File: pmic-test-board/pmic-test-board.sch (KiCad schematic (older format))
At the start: 53 parts

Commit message: more schematic capture
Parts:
- added C106: DNP, Capacitor_SMD:C_0603_1608Metric, symbol Device:C
- added C? (x2): 4.7u, Capacitor_SMD:C_0603_1608Metric, symbol Device:C
- added J?: Conn_02x09_Odd_Even, symbol Connector_Generic:Conn_02x09_Odd_Even
- added J?: Conn_Coaxial, symbol Connector:Conn_Coaxial
- added R?: 1k, Resistor_SMD:R_0603_1608Metric, symbol Device:R
- added R? (x6): 4.7k, symbol Device:R
- added R? (x4): 100, symbol Device:R
- C101: renamed from C?; footprint (none) -> Capacitor_SMD:C_0603_1608Metric
- C102: renamed from C?; footprint (none) -> Capacitor_Tantalum_SMD:CP_EIA-3528-12_Kemet-T; MPN (none) -> T520B476M008ATE035
- C104: renamed from C?; value C -> 5.1n; footprint (none) -> Capacitor_SMD:C_0603_1608Metric
- C105: renamed from C?; value C -> 220p; footprint (none) -> Capacitor_SMD:C_0603_1608Metric
- D101, D102, D103, D104, D105, D106: renamed from D?; footprint (none) -> LED_SMD:LED_0603_1608Metric_Castellated
- D107, D108: renamed from D?; value D_Schottky -> B0520WS-7-F; footprint (none) -> Diode_SMD:D_SOD-323; MPN (none) -> B0520WS-7-F
- L101: renamed from L?; value L -> 22u; MPN (none) -> LPS6235-223MRC
- Q101, Q102, Q103, Q104: renamed from Q?; footprint (none) -> Package_TO_SOT_SMD:SOT-23
- R101, R102, R103, R104, R105, R106, R107, R108, R109, R110, R111, R112, R113, R114, R115, R116, R117, R118, R119: renamed from R?; footprint (none) -> Resistor_SMD:R_0603_1608Metric
- R120: renamed from R?; value R -> 17.6k; footprint (none) -> Resistor_SMD:R_0603_1608Metric
- R121: renamed from R?; value R -> 40k; footprint (none) -> Resistor_SMD:R_0603_1608Metric
- R122: renamed from R?; value R -> 7.8k; footprint (none) -> Resistor_SMD:R_0603_1608Metric
- U101, U102: renamed from U?; footprint (none) -> Package_TO_SOT_SMD:SOT-363_SC-70-6
- U103: renamed from U?; MPN (none) -> W25Q32JVSSIQ
- gave numbers to parts that had none: 11
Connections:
- net +3V3: now also U103.8 (VCC), C?.1, C?.1
- net GND: now also U103.4 (GND), C106.2, C?.2, C?.2, J?.1 (In), R?.1, R?.1, R?.1, R?.1, R?.1, R?.1
- net vsw: now also D107.2 (A), D108.1 (K), L101.1, R119.1, J?.2 (Ext)
- net at U103.1 (~CS): now also R?.1, R?.2
- net at U103.2 (DO(IO1)): now also R?.2, R?.2
- net at U103.3 (IO2): now also R?.2
- net at U103.5 (DI(IO0)): now also R?.2, R?.2
- net at U103.6 (CLK): now also R?.1, R?.2
- net at U103.7 (IO3): now also R?.2
- net at SW101.7: now also R?.1
- net flash_~CS: now reaches U104.24 (flash_csb)
- net flash_~CS: now also R?.2
- net flash_clk: now reaches U104.25 (flash_clk)
- net flash_clk: now also R?.2
- net flash_io0: now reaches U104.26 (flash_io0)
- net flash_io0: now also R?.1
- net flash_io1: now reaches U104.27 (flash_io1)
- net flash_io1: now also R?.1
- net at R120.2, R121.1: now also C106.1
- net load_sw_en: now reaches J104.2 (Ext), R105.1, U102.3
- net load_sw_en: now also R?.2
- new net FTDI_5V: J?.2 (Pin_2)
- new net FTDI_C0: J?.10 (Pin_10)
- new net FTDI_C1: J?.9 (Pin_9)
- new net FTDI_C2: J?.8 (Pin_8)
- new net FTDI_C3: J?.7 (Pin_7)
- new net FTDI_C4: J?.6 (Pin_6)
- new net FTDI_C5: J?.5 (Pin_5)
- new net FTDI_C6: J?.4 (Pin_4)
- new net FTDI_C7: J?.3 (Pin_3)
- new net FTDI_D0: J?.18 (Pin_18)
- new net FTDI_D1: J?.17 (Pin_17)
- new net FTDI_D2: J?.16 (Pin_16)
- new net FTDI_D3: J?.15 (Pin_15)
- new net FTDI_D4: J?.14 (Pin_14)
- new net FTDI_D5: J?.13 (Pin_13)
- new net FTDI_D6: J?.12 (Pin_12)
- new net FTDI_D7: J?.11 (Pin_11)
- new net FTDI_GND: J?.1 (Pin_1)
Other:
- note added: "Pin header to plug in UM232H-B breakout PCB"
- note added: "scope probe testpoint"
- moved on the sheet: C102, C103, J103, J104, L101, R104, R105, R117, R118, R120, R121, SW102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

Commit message: PCB routing done
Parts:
- removed D103: LED, LED_SMD:LED_0603_1608Metric_Castellated, symbol Device:LED
- removed J105, J106: Conn_01x02_Female, symbol Connector:Conn_01x02_Female
- removed Q101: BSR202N, Package_TO_SOT_SMD:SOT-23, symbol Device:Q_NMOS_GSD
- removed R?: 1k, Resistor_SMD:R_0603_1608Metric, symbol Device:R
- added C108, C109, C110, C111, C112, C113, C115, C116, C117, C118, C119: 4.7u, Capacitor_SMD:C_0603_1608Metric, symbol Device:C
- added C120, C121: 0.47u, Capacitor_SMD:C_0603_1608Metric, symbol Device:C
- added D109, D110: LED, LED_SMD:LED_0603_1608Metric_Castellated, symbol Device:LED
- added J105: Conn_01x02_Male, Connector_PinHeader_2.54mm:PinHeader_1x02_P2.54mm_Vertical, symbol Connector:Conn_01x02_Male
- added J106, J107: Conn_01x04_Male, Connector_PinHeader_2.54mm:PinHeader_1x04_P2.54mm_Vertical, symbol Connector:Conn_01x04_Male
- added J110: Conn_Coaxial, Connector_Coaxial:SMA_Amphenol_132134_Vertical, symbol Connector:Conn_Coaxial
- added J113: Conn_01x04_Female, wbraun_smd:Terminal-block-plug_4x1_3.5mm-pitch, symbol Connector:Conn_01x04_Female
- added J114: Conn_Coaxial, wbraun_smd:PK007-015, symbol Connector:Conn_Coaxial
- added J115, J116, J117, J118: mounting-hole-nc, wbraun_smd:M3-mounting-hole-insulated, symbol wbraun_ic_lib:mounting-hole-nc
- added R126, R128: 1k, Resistor_SMD:R_0603_1608Metric, symbol Device:R
- added R131, R132, R133, R134, R143, R144, R145, R146: 47, Resistor_SMD:R_0603_1608Metric, symbol Device:R
- added R139: R, Resistor_SMD:R_1206_3216Metric, symbol Device:R
- added R140, R141, R142: 0, Resistor_SMD:R_0603_1608Metric, symbol Device:R
- added R147, R148: 4.7k, Resistor_SMD:R_0603_1608Metric, symbol Device:R
- added R149: 20, Resistor_SMD:R_0603_1608Metric, symbol Device:R
- added TP101, TP102, TP103, TP104, TP105, TP106: TestPoint, wbraun_smd:THM_COMPACT, symbol Connector:TestPoint
- C103: footprint (none) -> Capacitor_SMD:C_0805_2012Metric
- J101, J102, J103: footprint (none) -> wbraun_smd:CONN_SMA_EDGE_SAMTEC_SMA_J_P_H_ST_EM1
- J104: footprint (none) -> wbraun_smd:CONN_SMA_EDGE_SAMTEC_SMA_J_P_H_ST_EM1; MPN (none) -> SMA-J-P-H-ST-EM1
- J108: renamed from J?; footprint (none) -> Connector_PinHeader_2.54mm:PinHeader_2x09_P2.54mm_Vertical
- J109: renamed from J?; footprint (none) -> wbraun_smd:PK007-015
- L101: footprint (none) -> wbraun_smd:L_Wuerth_WE-PD-Typ-7345; MPN LPS6235-223MRC -> 7447779122
- R107: value 1k -> DNP
- R123, R124, R125, R127, R129, R130, R135, R136, R137, R138: renamed from R?; footprint (none) -> Resistor_SMD:R_0603_1608Metric
- SW101: footprint (none) -> Button_Switch_THT:SW_DIP_SPSTx08_Slide_6.7x21.88mm_W7.62mm_P2.54mm_LowProfile; MPN (none) -> DS01C-254-S-08BE
- SW102: footprint (none) -> wbraun_smd:SW_SPST_PTS810; MPN (none) -> PTS810 SJK 250 SMTR LFS
- gave numbers to parts that had none: 2
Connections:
- net +1V8: now also C112.1, R140.1
- net +3V3: now also C108.1, C109.1, C110.1, C120.1, C121.1, J106.1 (Pin_1), J107.1 (Pin_1), R126.1, R128.1, R147.2, R148.2; no longer R107.1
- net BUCK_PWR: now also C115.1, C116.1
- net CTRL_PWR: now also R141.2, TP103.1; no longer U104.40 (vdda1), U104.47 (vdda1), U104.9 (vdda2)
- net FTDI_C2: now also D109.1 (K)
- net FTDI_C3: now also D110.1 (K)
- net FTDI_D0: now also R131.2
- net FTDI_D1: now also R133.2
- net FTDI_D2: now also R134.2
- net FTDI_D4: now also R132.2
- net GND: now also J101.2 (Ext), J102.2 (Ext), J103.2 (Ext), J104.2 (Ext), J109.2 (Ext), R102.1, R104.1, C108.2, C109.2, C110.2, C111.2, C112.2, C113.2, C115.2, C116.2, C117.2, C118.2, C119.2, C120.2, C121.2, J106.4 (Pin_4), J107.4 (Pin_4), J110.2 (Ext), J113.3 (Pin_3), J113.4 (Pin_4), J114.2 (Ext); no longer J101.1 (In), J102.1 (In), J103.1 (In), J104.1 (In), J109.1 (In), R102.2, R104.2
- net osc_monitor: now also J114.1 (In)
- net user_vcore: now also C111.1, C113.1, R140.2
- net vcomp: now also R107.2, TP101.1
- net vfb: now also C106.1, R107.1, R120.2, R121.1
- net vsw: now also J109.1 (In), R139.1; no longer J109.2 (Ext)
- net HOST_SDO: now reaches U104.32 (mprj_io[1]_SDO)
- net HOST_SDO: now also R134.1
- net HOST_SDI: now reaches U104.33 (mprj_io[2]_SDI)
- net HOST_SDI: now also R133.1
- net HOST_CSB: now reaches U104.34 (mprj_io[3]_CSB)
- net HOST_CSB: now also R132.1, R147.1
- net HOST_SCK: now reaches U104.35 (mprj_io[4]_SCK)
- net HOST_SCK: now also R131.1
- net SER_RX: now reaches U104.36 (mprj_io[5]_ser_rx)
- net SER_RX: now also J106.2 (Pin_2), R148.1
- net SER_TX: now reaches U104.37 (mprj_io[6]_ser_tx)
- net SER_TX: now also J106.3 (Pin_3)
- net BUCK_VOUT: now reaches C102.1, C103.1
- net BUCK_VOUT: now also J105.2 (Pin_2), J113.1 (Pin_1), J113.2 (Pin_2), R142.1, R149.1, TP102.1, TP105.1; no longer L101.2, R120.1
- net at R103.1, U101.3: now also R144.1; no longer J102.2 (Ext)
- net imon renamed IMON
- net load_sw_en: no longer names the net of R105.1, U102.3
- net load_sw_en: now also R146.1; no longer J104.2 (Ext)
- net vref renamed VREF
- new net: J101.1 (In), R143.2
- new net: J105.1 (Pin_1), L101.2, R142.2
- new net: R120.1, R149.2, TP106.1
- new net: R102.2, R143.1, U101.1
- new net: J102.1 (In), R144.2
- new net: J103.1 (In), R145.2
- new net: R104.2, R145.1, U102.1
- new net: J104.1 (In), R146.2
- new net: D110.2 (A), R128.2
- new net: D109.2 (A), R126.2
- new net: J110.1 (In), R139.2
- new net CTRL_PRW_INJ: C117.1, C118.1, C119.1, R141.1, TP104.1, U104.40 (vdda1), U104.47 (vdda1), U104.9 (vdda2)
- new net SCL: J107.3 (Pin_3)
- new net SDA: J107.2 (Pin_2)
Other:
- note added: "Bode Injection Point"
- note added: "Injection point for current sense testing"
- note added: "bode injection points for PSRR"
- note added: "connection for \nopen loop gain test"
- moved on the sheet: C102, C103, C104, C105, C106, J108, J109, R102, R103, R104, R105, R118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

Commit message: schematic review and gerber generation
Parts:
- added TP107, TP108, TP109, TP110, TP111: TestPoint, wbraun_smd:THM_COMPACT, symbol Connector:TestPoint
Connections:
- net GND: now also TP111.1
- net LOAD_SW: now also TP110.1
- net nmos_val: now also TP107.1
- net pmos_val: now also TP109.1
- net timeout_ext: now also TP108.1
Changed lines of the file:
@@
 Wire Wire Line
 	11950 5800 11950 5500
+$Comp
+L Connector:TestPoint TP107
+U 1 1 61C0F9EF
+P 3100 7550
+F 0 "TP107" H 3158 7668 50  0000 L CNN
+F 1 "TestPoint" H 3158 7577 50  0000 L CNN
+F 2 "wbraun_smd:THM_COMPACT" H 3300 7550 50  0001 C CNN
+F 3 "~" H 3300 7550 50  0001 C CNN
+	1    3100 7550
+	1    0    0    -1
+$EndComp
+$Comp
+L Connector:TestPoint TP109
+U 1 1 61C10B95
+P 3800 7550
+F 0 "TP109" H 3858 7668 50  0000 L CNN
+F 1 "TestPoint" H 3858 7577 50  0000 L CNN
+F 2 "wbraun_smd:THM_COMPACT" H 4000 7550 50  0001 C CNN
+F 3 "~" H 4000 7550 50  0001 C CNN
+	1    3800 7550
+	1    0    0    -1
+$EndComp
+$Comp
+L Connector:TestPoint TP108
+U 1 1 61C38F9B
+P 3100 8050
+F 0 "TP108" H 3158 8168 50  0000 L CNN
+F 1 "TestPoint" H 3158 8077 50  0000 L CNN
+F 2 "wbraun_smd:THM_COMPACT" H 3300 8050 50  0001 C CNN
+F 3 "~" H 3300 8050 50  0001 C CNN
+	1    3100 8050
+	1    0    0    -1
+$EndComp
+$Comp
+L Connector:TestPoint TP110
+U 1 1 61C392C2
+P 3800 8050
+F 0 "TP110" H 3858 8168 50  0000 L CNN
+F 1 "TestPoint" H 3858 8077 50  0000 L CNN
+F 2 "wbraun_smd:THM_COMPACT" H 4000 8050 50  0001 C CNN
+F 3 "~" H 4000 8050 50  0001 C CNN
+	1    3800 8050
+	1    0    0    -1
+$EndComp
+Text Label 3100 7650 0    50   ~ 0
+nmos_val
+Text Label 3800 7650 0    50   ~ 0
+pmos_val
+Text Label 3100 8150 0    50   ~ 0
+timeout_ext
+Text GLabel 3800 8150 2    50   Input ~ 0
+LOAD_SW
+Wire Wire Line
+	3800 8150 3800 8050
+Wire Wire Line
+	3100 8150 3100 8050
+Wire Wire Line
+	3100 7650 3100 7550
+Wire Wire Line
+	3800 7650 3800 7550
+$Comp
+L Connector:TestPoint TP?
+U 1 1 61CFBA11
+P 3550 8700
+AR Path="/61A0E07B/61CFBA11" Ref="TP?"  Part="1"
+AR Path="/61CFBA11" Ref="TP111"  Part="1"
+F 0 "TP111" H 3608 8818 50  0000 L CNN
+F 1 "TestPoint" H 3608 8727 50  0000 L CNN
+F 2 "wbraun_smd:THM_COMPACT" H 3750 8700 50  0001 C CNN
+F 3 "~" H 3750 8700 50  0001 C CNN
+	1    3550 8700
+	1    0    0    -1
+$EndComp
+$Comp
+L power:GND #PWR?
+U 1 1 61CFBA17
+P 3550 8750
+AR Path="/61A0E07B/61CFBA17" Ref="#PWR?"  Part="1"
+AR Path="/61CFBA17" Ref="#PWR0188"  Part="1"
+F 0 "#PWR0188" H 3550 8500 50  0001 C CNN
+F 1 "GND" H 3555 8577 50  0000 C CNN
+F 2 "" H 3550 8750 50  0001 C CNN
+F 3 "" H 3550 8750 50  0001 C CNN
+	1    3550 8750
+	1    0    0    -1
+$EndComp
+Wire Wire Line
+	3550 8750 3550 8700
 $EndSCHEMATC

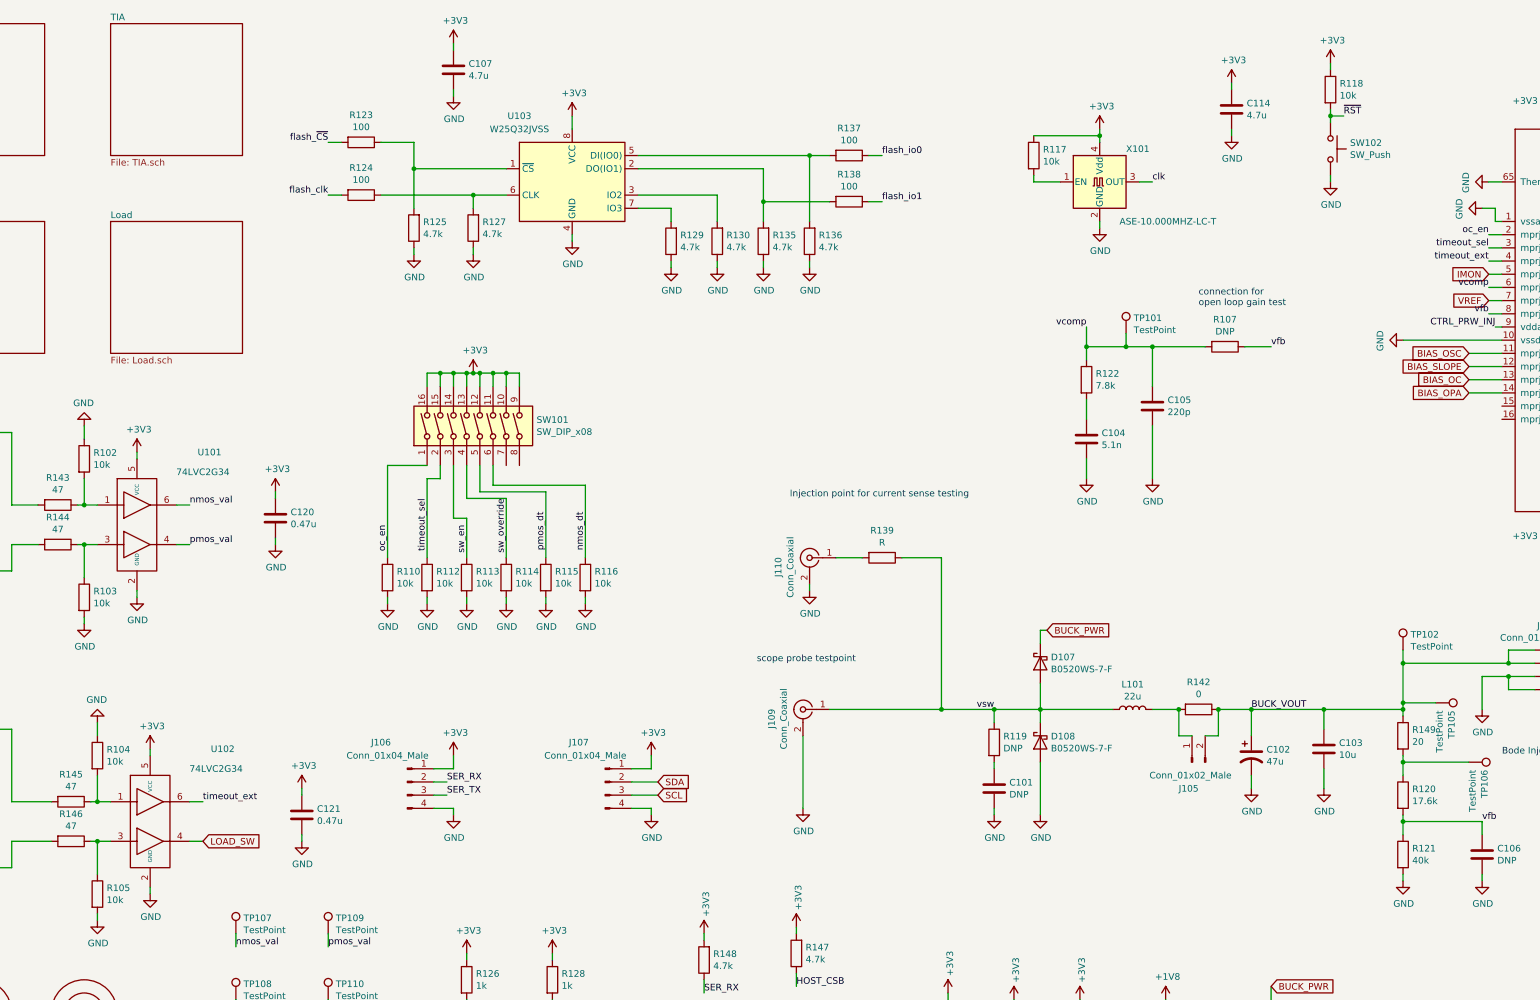
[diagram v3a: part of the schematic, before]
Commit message: added test firmware and test results
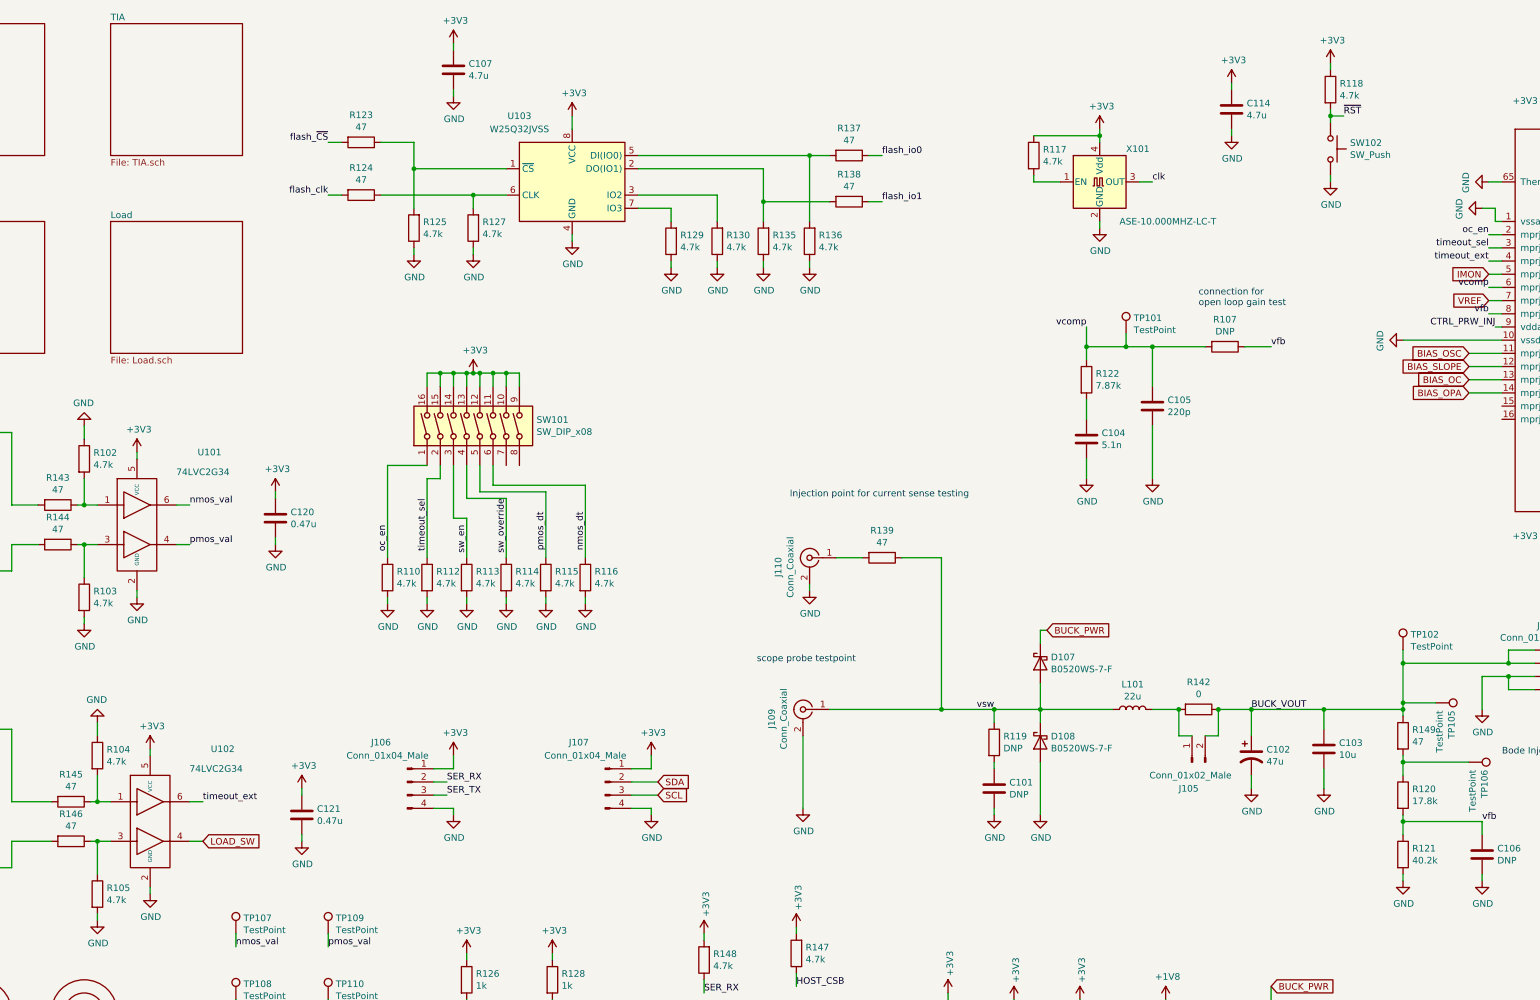
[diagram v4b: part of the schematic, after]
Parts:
- C102: MPN T520B476M008ATE035 -> T520B476M010ATE035
- C103: MPN (none) -> CL21B106KPQNFNE
- C104: MPN (none) -> C0603X512J5JAC7867
- C105: MPN (none) -> CC0603KRX7R0BB221
- C107, C108, C109, C110, C111, C112, C113, C114, C115, C116, C117, C118, C119: MPN (none) -> CL10A475MO8NNNC
- C120, C121: MPN (none) -> CL10B474KO8NFNC
- J101, J102, J103: MPN (none) -> SMA-J-P-H-ST-EM1
- J108: MPN (none) -> PH2-18-UA
- R101, R106, R108, R109, R111, R126, R128: MPN (none) -> RMCF0603FG1K00
- R102, R103, R104, R105, R110, R112, R113, R114, R115, R116, R117, R118: value 10k -> 4.7k; MPN (none) -> RMCF0603FT4K70
- R120: value 17.6k -> 17.8k; MPN (none) -> RMCF0603FG17K8
- R121: value 40k -> 40.2k; MPN (none) -> RMCF0603FT40K2
- R122: value 7.8k -> 7.87k; MPN (none) -> RMCF0603FT7K87
- R123, R124, R137, R138: value 100 -> 47; MPN (none) -> RMCF0603FT47R0
- R125, R127, R129, R130, R135, R136, R147, R148: MPN (none) -> RMCF0603FT4K70
- R131, R132, R133, R134, R143, R144, R145, R146: MPN (none) -> RMCF0603FT47R0
- R139: value R -> 47; MPN (none) -> RMCF1206FT47R0
- R140, R141, R142: MPN (none) -> RC0603JR-070RL
- R149: value 20 -> 47; MPN (none) -> RMCF0603FT47R0
- TP101, TP102, TP103, TP104, TP105, TP106, TP107, TP108, TP109, TP110, TP111: MPN (none) -> 5119
- U101, U102: MPN (none) -> 74LVC2G34GW,125
